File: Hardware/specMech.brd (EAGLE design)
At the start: 142.2 x 121.9 mm, 73 parts, among them IC1 MCP23008, J1 Molex 0022232081, J2 Molex 0022232081, J3 PINHD-1X8-MOLEX-SHROUD, J4 PINHD-1X8-MOLEX-SHROUD, J5 XPORT, J6 Molex 0022232081, J7 Molex 0022232081, J8 Molex 0022232081, U1 MCP23008-E/SO, U10 ADS1115, U2 MCP23008-E/SO, U3 TXB0102DCURVSSOP8, U4 MCP9808-E/MS, U5 TBD62083, U6 TBD62083SOP18-P-375-1.27, U7 MCP23008-E/SO, U8 MCP23008-E/SO, U9 ADS1115

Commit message: Worked on board layout
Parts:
- removed C1: 0.1uF, AUmlib:C0805
- removed IC1: MCP23008, AUmlib:SOIC127P1032X265-18
- removed J1: Molex 0022232081, AUmlib:1X08-MOLEX-SHROUD
- removed JP5: (no value), AUmlib:1X02
- removed R1, R12, R17, R18, R19, R20, R21, R23, R24, R25, R26: 10K, AUmlib:R0805
- removed U6: TBD62083SOP18-P-375-1.27, AUmlib:SOIC127P1030X245-18
- removed U7: MCP23008-E/SO, AUmlib:SOIC18-W_MC
- added C21: 0.1uF, AUmlib:C0805
- added RN1, RN2: EXB-38V103JV, AUmlib:EXB38V_PAN
- added U11: MCP23008-E/SO, AUmlib:SOIC18-W_MC
- R15, R4: value 4K7 -> 10K
- moved C20 327.3 mm to (116.8, 5.08), turned to 270 degrees
- moved C18 316.4 mm to (127.0, 5.08), turned to 270 degrees
- moved C19 315.2 mm to (127.0, 10.2), turned to 270 degrees
- moved U10 311.3 mm to (121.9, 12.7)
- moved C16 307.8 mm to (116.8, 33.0), turned to 90 degrees
- moved C17 301.1 mm to (116.8, 10.2), turned to 270 degrees
- moved C15 292.8 mm to (116.8, 27.9), turned to 270 degrees
- moved R16 283.9 mm to (127.0, 33.0), turned to 90 degrees
- moved C13 277.7 mm to (127.0, 15.2), turned to 90 degrees
- moved R27 275.5 mm to (-27.9, 25.4)
- moved R4 267.4 mm to (88.9, 38.1), turned to 270 degrees
- moved C12 265.8 mm to (127.0, 38.1), turned to 90 degrees
- moved C14 264.2 mm to (127.0, 27.9), turned to 270 degrees
- moved R22 258.2 mm to (-17.8, 35.6)
- moved R15 252.7 mm to (88.9, 33.0), turned to 90 degrees
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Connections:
- removed net /RST: IC1.6, R17.2
- removed net AIN1: C14.1, R19.2, U9.5
- removed net AIN2: C17.1, R24.2, U10.5
- removed net INT: IC1.8, R18.2
- removed net N$19: J1.P$5, U6.15
- removed net N$23: J1.P$4, U6.14
- removed net N$25: J1.P$3, U6.13
- removed net N$26: J1.P$2, U6.12
- removed net N$27: J1.P$1, U6.11
- removed net N$28: U6.8, U7.10
- removed net N$29: U6.7, U7.11
- removed net N$30: U6.6, U7.12
- removed net N$31: U6.5, U7.13
- removed net N$32: U6.4, U7.14
- removed net N$33: U6.3, U7.15
- removed net N$34: U6.2, U7.16
- removed net N$35: U6.1, U7.17
- removed net N$58: R1.1, U7.6
- removed net N$59: R12.1, U7.8
- removed net N$6: J1.P$8, U6.18
- removed net N$7: J1.P$7, U6.17
- removed net N$8: J1.P$6, U6.16
- removed net PUP: JP5.1, R15.2, R4.2
- new net A0B: J4.P$8, RN1.8
- new net A1B: J4.P$6, RN1.7
- new net A2B: J4.P$4, RN1.6
- new net A3B: J4.P$2, RN1.5
- new net N$69: C17.1, RN1.1, U10.4
- new net N$70: R27.2, U10.1, U10.2
- new net N$71: J3.P$5, U11.14
- new net N$72: J3.P$7, U11.16
- net +12V: no longer U6.10
- net +5V: now also C21.1, R4.1, U11.18; no longer C1.1, IC1.18, JP5.2, R1.2, R17.1, U7.18
- net A0A: now also RN2.8; no longer R21.1, R26.1
- net A1A: now also RN2.7; no longer R19.1, R24.1
- net A2A: now also RN2.6; no longer C20.1, J3.P$2, J3.P$4, J3.P$6, J3.P$8, R16.1, R23.2, U10.6, U9.6
- net A3A: now also J3.P$2, J3.P$4, J3.P$6, J3.P$8, R16.1, U9.7; no longer R20.1, R25.1
- net GND: now also C21.2, J4.P$1, J4.P$3, J4.P$5, J4.P$7, R15.1, U11.3, U11.4, U11.5, U11.9; no longer C1.2, IC1.3, IC1.4, IC1.5, IC1.9, R12.2, R18.1, U10.1, U6.9, U7.3, U7.4, U7.5, U7.9
- net N$18: now also R15.2, U11.8; no longer IC1.12, J3.P$5
- net N$5: now also R4.2, U11.6; no longer IC1.10, J3.P$7
- net N$60: now also J3.P$1, U11.10; no longer IC1.14, J3.P$3
- net N$61: now also J3.P$3, U11.12; no longer IC1.16, J3.P$1
- net N$62: now also C16.1, RN2.1, U9.4; no longer C15.1, R20.2, U9.7
- net N$63: now also C15.1, RN2.2, U9.5; no longer C16.1, R21.2, U9.4
- net N$65: now also RN1.4, U10.7; no longer R26.2, U10.4
- net N$66: now also C14.1, RN2.3, U9.6; no longer R27.2, U10.2
- net N$67: now also RN1.3, U10.6; no longer R25.2, U10.7
- net N$68: now also C20.1, RN1.2, U10.5; no longer R23.1
- net SCL: now also U11.1; no longer IC1.1, R15.1, U7.1
- net SDA: now also U11.2; no longer IC1.2, R4.1, U7.2

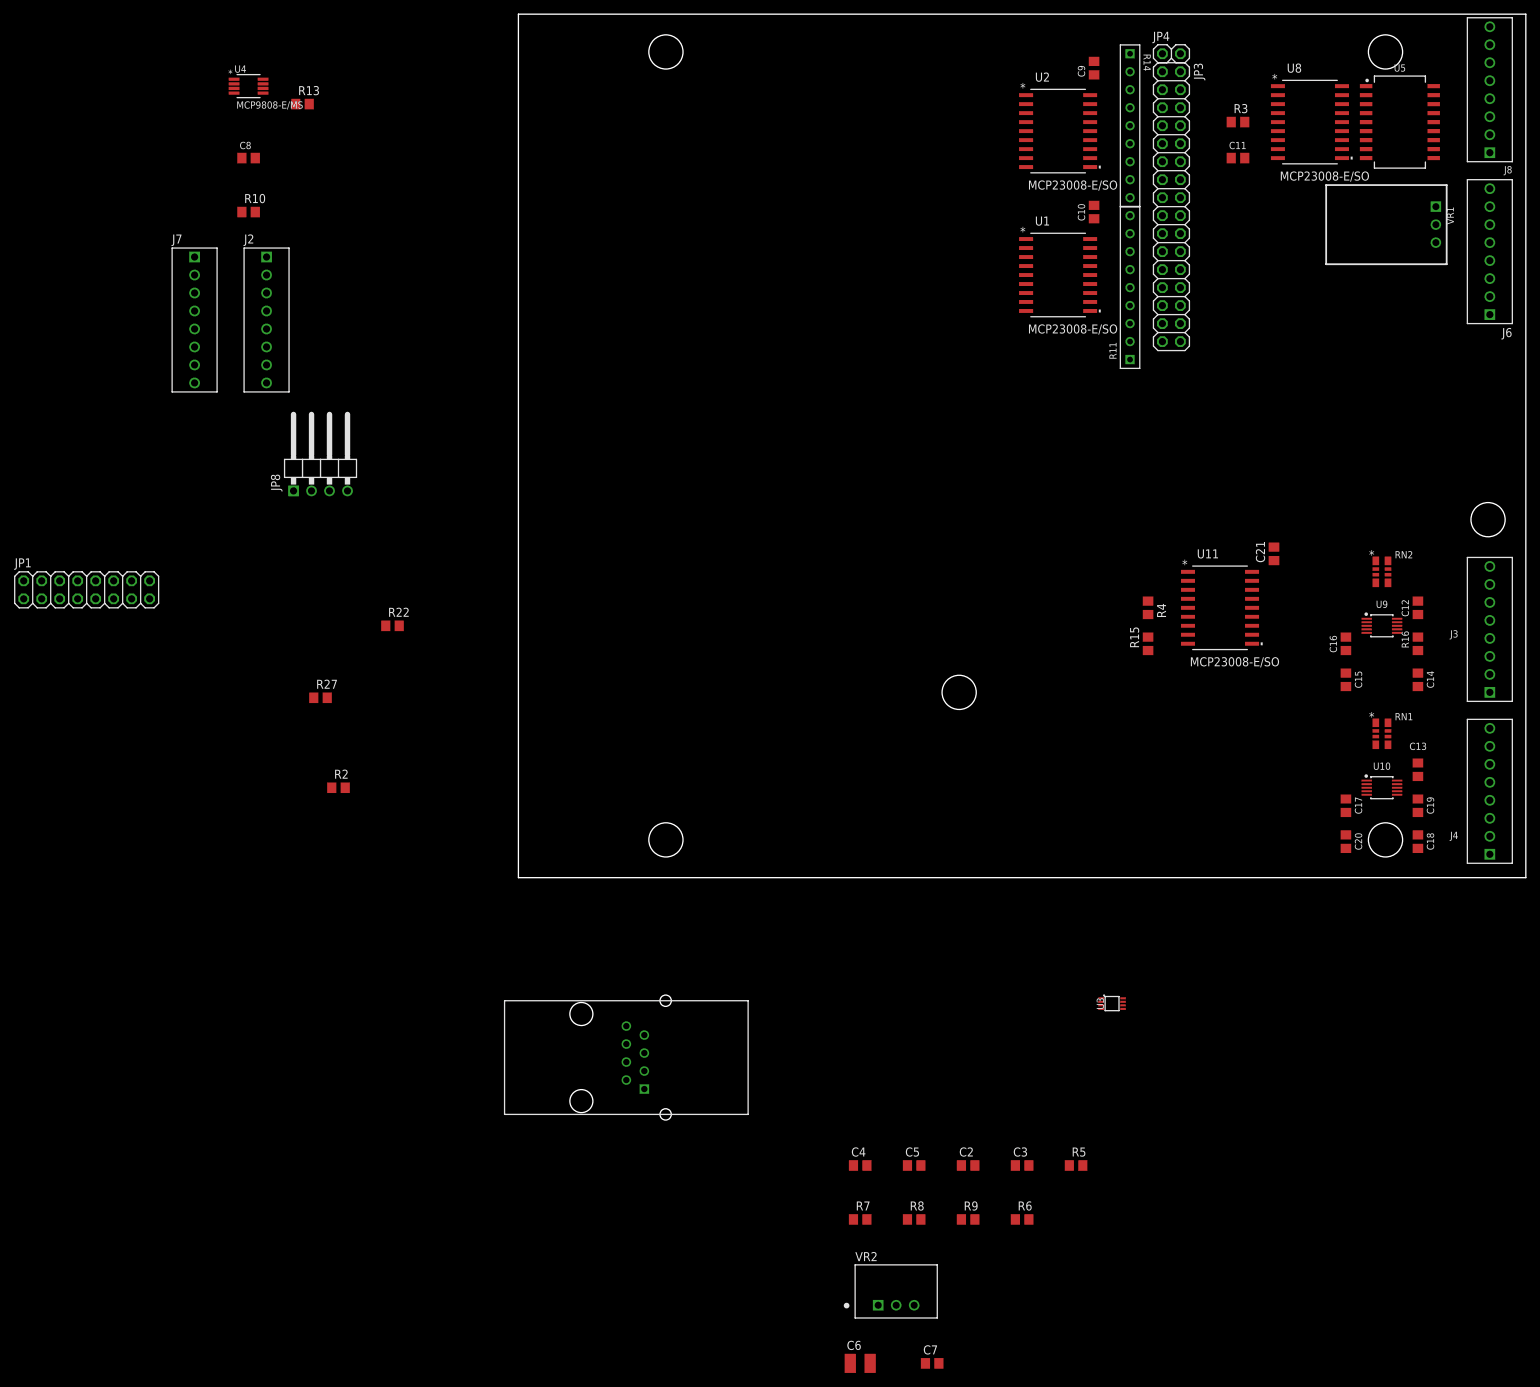
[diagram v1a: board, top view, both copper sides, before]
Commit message: Remove backup Eagle files
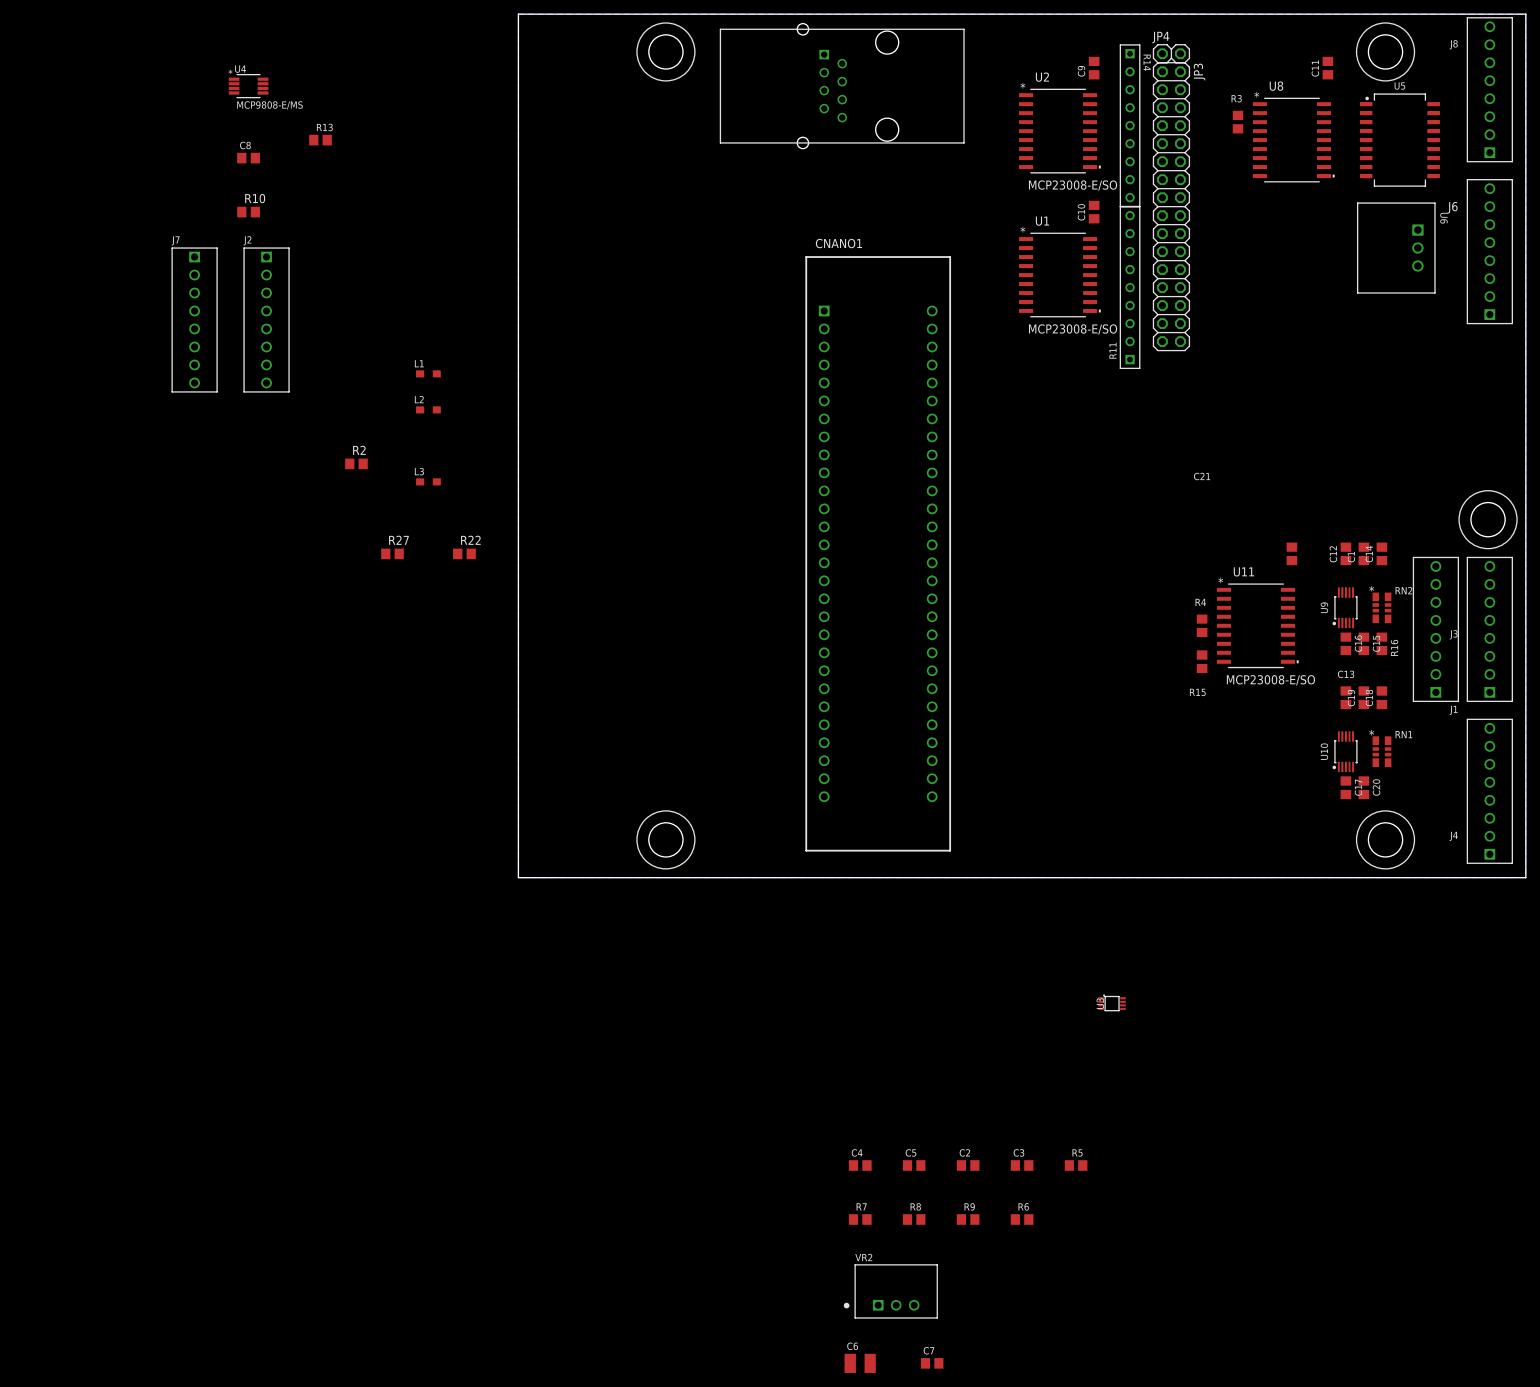
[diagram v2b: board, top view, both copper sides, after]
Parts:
- removed JP1: (no value), AUmlib:2X08
- removed JP8: (no value), AUmlib:1X04/90
- removed VR1: OKI-78SR, AUmlib:OKI-78SR
- added C1: 0.01uF, AUmlib:C0805
- added CNANO1: CURIOSITYNANO4809, AUmlib:CURIOSITYNANO4809
- added J1: PINHD-1X8-MOLEX-SHROUD, AUmlib:1X08-MOLEX-SHROUD
- added L1, L2, L3: MMZ2012Y152BT000, AUmlib:INDC2012X87N
- added U6: OKI-78SR-5/1.5-W36E-C, AUmlib:OKI-78SR-5/1.5-W36E-C_MUR
- moved J5 140.5 mm to (45.7, 111.8), turned to 180 degrees
- moved R2 45.8 mm to (-22.9, 58.4)
- moved R27 22.7 mm to (-17.8, 45.7)
- moved C18 20.9 mm to (121.9, 25.4), turned to 90 degrees
- moved C14 18.5 mm to (121.9, 45.7), turned to 90 degrees
- moved C11 18.0 mm to (114.3, 114.3), turned to 90 degrees
- moved C19 17.0 mm to (119.4, 25.4), turned to 90 degrees
- moved R22 14.4 mm to (-7.62, 45.7)
- moved C13 14.4 mm to (116.8, 25.4)
- moved C12 12.7 mm to (116.8, 45.7)
- moved C20 8.03 mm to (119.4, 12.7)
- moved R15 8.03 mm to (96.5, 30.5)
- moved R4 8.03 mm to (96.5, 35.6)
- moved U10 7.18 mm to (116.8, 17.8), turned to 90 degrees
- moved C15 5.68 mm to (119.4, 33.0)
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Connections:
- new net GND-ISO: C1.2, C14.2, C15.2, C16.2, C17.2, C18.2, C19.2, C20.2, L3.2, R16.2, U10.3, U9.3
- new net N$6: C13.1, L2.1, R27.1, U10.8
- new net N$7: C12.1, L1.1, R22.1, U9.8
- net +12V: now also U6.1; no longer VR1.VIN
- net +5V: now also L1.2, L2.2, U6.3; no longer C12.1, C13.1, JP8.3, R22.1, R27.1, U10.8, U9.8, VR1.VOUT
- net A0A: now also J1.P$8
- net A1A: now also J1.P$6
- net A2A: now also J1.P$4
- net A3A: now also C1.1, J1.P$2, RN2.4, RN2.5
- net GND: now also J1.P$1, J1.P$3, J1.P$5, J1.P$7, L3.1, U6.2; no longer C14.2, C15.2, C16.2, C17.2, C18.2, C19.2, C20.2, JP8.1, R16.2, U10.3, U9.3, VR1.GND
- net SCL: no longer JP8.4
- net SDA: no longer JP8.2
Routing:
- added copper zone on layer 16, net GND
